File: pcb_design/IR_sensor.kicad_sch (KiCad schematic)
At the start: 32 parts, among them J6 IR_1, J7 IR_1, J8 IR_2, J9 IR_1, Q2 DMN3065LW-7, Q3 DMN3065LW-7, Q4 DMN3065LW-7, Q5 DMN3065LW-7

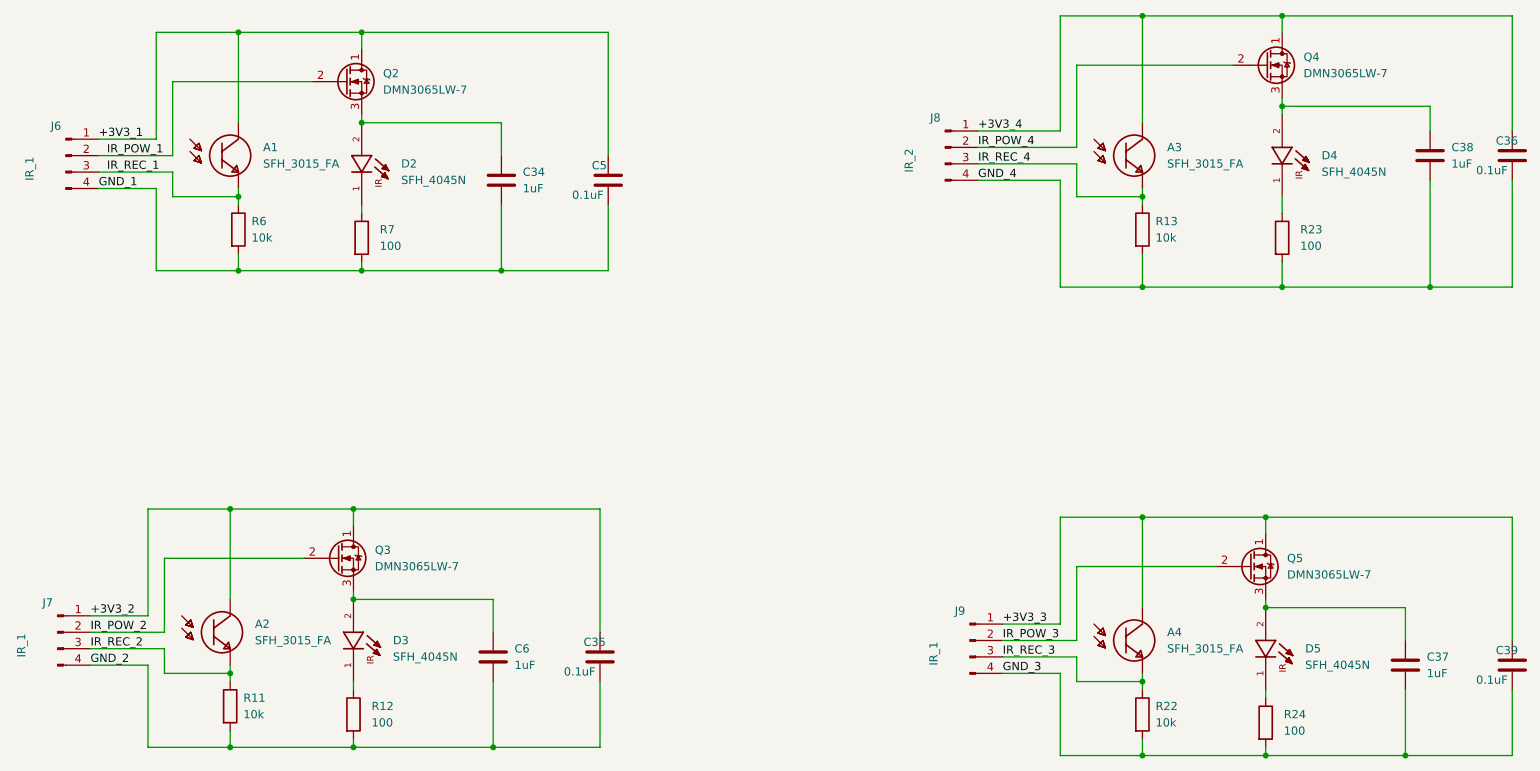
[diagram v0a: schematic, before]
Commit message: Add changes to silkscreen and filter capacitors
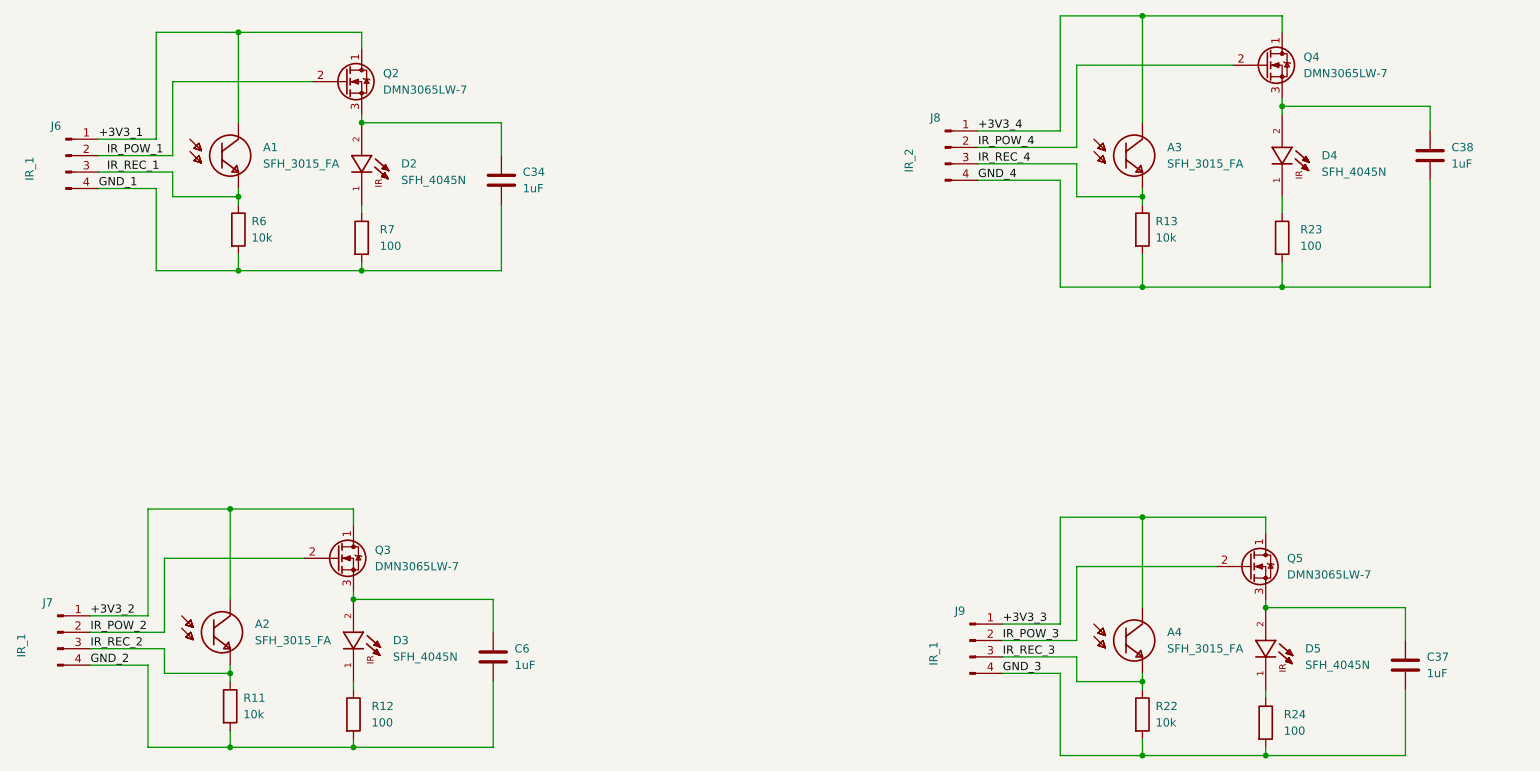
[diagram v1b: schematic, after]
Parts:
- removed C35, C36, C39, C5: 0.1uF, Capacitor_SMD:C_0402_1005Metric, symbol Device:C
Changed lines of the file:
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@@
   (junction (at 224.79 76.2) (diameter 0) (color 0 0 0 0)
   )
-  (junction (at 222.25 111.76) (diameter 0) (color 0 0 0 0)
-  )
   (junction (at 63.5 62.23) (diameter 0) (color 0 0 0 0)
   )
-  (junction (at 82.55 36.83) (diameter 0) (color 0 0 0 0)
-  )
-  (junction (at 104.14 73.66) (diameter 0) (color 0 0 0 0)
-  )
   (junction (at 62.23 135.89) (diameter 0) (color 0 0 0 0)
   )
@@
   (junction (at 63.5 36.83) (diameter 0) (color 0 0 0 0)
   )
-  (junction (at 81.28 110.49) (diameter 0) (color 0 0 0 0)
-  )
   (junction (at 203.2 148.59) (diameter 0) (color 0 0 0 0)
   )
-  (junction (at 224.79 34.29) (diameter 0) (color 0 0 0 0)
-  )
   (junction (at 203.2 34.29) (diameter 0) (color 0 0 0 0)
   )
-  (junction (at 102.87 147.32) (diameter 0) (color 0 0 0 0)
-  )
-  (junction (at 247.65 76.2) (diameter 0) (color 0 0 0 0)
-  )
   (junction (at 224.79 48.26) (diameter 0) (color 0 0 0 0)
   )
@@
   (junction (at 82.55 73.66) (diameter 0) (color 0 0 0 0)
   )
-  (junction (at 243.84 148.59) (diameter 0) (color 0 0 0 0)
-  )
   (wire (pts (xy 81.28 110.49) (xy 81.28 113.03))
     (stroke (width 0) (type default) (color 0 0 0 0))
@@
     (stroke (width 0) (type default) (color 0 0 0 0))
   )
-  (wire (pts (xy 119.38 147.32) (xy 102.87 147.32))
-    (stroke (width 0) (type default) (color 0 0 0 0))
-  )
   (wire (pts (xy 190.5 52.07) (xy 190.5 34.29))
     (stroke (width 0) (type default) (color 0 0 0 0))
@@
     (stroke (width 0) (type default) (color 0 0 0 0))
   )
-  (wire (pts (xy 260.35 138.43) (xy 260.35 148.59))
-    (stroke (width 0) (type default) (color 0 0 0 0))
-  )
   (wire (pts (xy 247.65 52.07) (xy 247.65 48.26))
     (stroke (width 0) (type default) (color 0 0 0 0))
@@
     (stroke (width 0) (type default) (color 0 0 0 0))
   )
-  (wire (pts (xy 224.79 34.29) (xy 260.35 34.29))
-    (stroke (width 0) (type default) (color 0 0 0 0))
-  )
-  (wire (pts (xy 120.65 73.66) (xy 104.14 73.66))
-    (stroke (width 0) (type default) (color 0 0 0 0))
-  )
   (wire (pts (xy 222.25 148.59) (xy 243.84 148.59))
     (stroke (width 0) (type default) (color 0 0 0 0))
   )
-  (wire (pts (xy 82.55 36.83) (xy 120.65 36.83))
-    (stroke (width 0) (type default) (color 0 0 0 0))
-  )
   (wire (pts (xy 104.14 55.88) (xy 104.14 50.8))
     (stroke (width 0) (type default) (color 0 0 0 0))
@@
     (stroke (width 0) (type default) (color 0 0 0 0))
   )
-  (wire (pts (xy 222.25 111.76) (xy 260.35 111.76))
-    (stroke (width 0) (type default) (color 0 0 0 0))
-  )
   (wire (pts (xy 203.2 111.76) (xy 222.25 111.76))
     (stroke (width 0) (type default) (color 0 0 0 0))
   )
-  (wire (pts (xy 119.38 137.16) (xy 119.38 147.32))
-    (stroke (width 0) (type default) (color 0 0 0 0))
-  )
   (wire (pts (xy 243.84 130.81) (xy 243.84 125.73))
     (stroke (width 0) (type default) (color 0 0 0 0))
@@
     (stroke (width 0) (type default) (color 0 0 0 0))
   )
-  (wire (pts (xy 260.35 59.69) (xy 260.35 76.2))
-    (stroke (width 0) (type default) (color 0 0 0 0))
-  )
   (wire (pts (xy 224.79 72.39) (xy 224.79 76.2))
     (stroke (width 0) (type default) (color 0 0 0 0))
@@
     (stroke (width 0) (type default) (color 0 0 0 0))
   )
-  (wire (pts (xy 260.35 130.81) (xy 260.35 111.76))
-    (stroke (width 0) (type default) (color 0 0 0 0))
-  )
   (wire (pts (xy 49.53 127) (xy 49.53 110.49))
     (stroke (width 0) (type default) (color 0 0 0 0))
@@
     (stroke (width 0) (type default) (color 0 0 0 0))
   )
-  (wire (pts (xy 260.35 148.59) (xy 243.84 148.59))
-    (stroke (width 0) (type default) (color 0 0 0 0))
-  )
   (wire (pts (xy 62.23 135.89) (xy 62.23 137.16))
     (stroke (width 0) (type default) (color 0 0 0 0))
@@
     (stroke (width 0) (type default) (color 0 0 0 0))
   )
-  (wire (pts (xy 120.65 63.5) (xy 120.65 73.66))
-    (stroke (width 0) (type default) (color 0 0 0 0))
-  )
   (wire (pts (xy 82.55 36.83) (xy 82.55 39.37))
     (stroke (width 0) (type default) (color 0 0 0 0))
@@
     (stroke (width 0) (type default) (color 0 0 0 0))
   )
-  (wire (pts (xy 81.28 110.49) (xy 119.38 110.49))
-    (stroke (width 0) (type default) (color 0 0 0 0))
-  )
   (wire (pts (xy 53.34 62.23) (xy 63.5 62.23))
     (stroke (width 0) (type default) (color 0 0 0 0))
@@
     (stroke (width 0) (type default) (color 0 0 0 0))
   )
-  (wire (pts (xy 260.35 76.2) (xy 247.65 76.2))
-    (stroke (width 0) (type default) (color 0 0 0 0))
-  )
   (wire (pts (xy 53.34 44.45) (xy 53.34 55.88))
     (stroke (width 0) (type default) (color 0 0 0 0))
@@
     (stroke (width 0) (type default) (color 0 0 0 0))
   )
-  (wire (pts (xy 119.38 129.54) (xy 119.38 110.49))
-    (stroke (width 0) (type default) (color 0 0 0 0))
-  )
   (wire (pts (xy 62.23 110.49) (xy 62.23 124.46))
     (stroke (width 0) (type default) (color 0 0 0 0))
@@
     (stroke (width 0) (type default) (color 0 0 0 0))
   )
-  (wire (pts (xy 260.35 52.07) (xy 260.35 34.29))
-    (stroke (width 0) (type default) (color 0 0 0 0))
-  )
   (wire (pts (xy 102.87 124.46) (xy 81.28 124.46))
     (stroke (width 0) (type default) (color 0 0 0 0))
@@
   )
   (wire (pts (xy 52.07 135.89) (xy 62.23 135.89))
-    (stroke (width 0) (type default) (color 0 0 0 0))
-  )
-  (wire (pts (xy 120.65 55.88) (xy 120.65 36.83))
     (stroke (width 0) (type default) (color 0 0 0 0))
   )
@@
     (pin "4")
   )
-  (symbol (lib_id "Device:C") (at 260.35 55.88 0) (unit 1)
-    (in_bom yes) (on_board yes)
-    (property "Reference" "C36" (id 0) (at 257.81 53.594 0)
-      (effects (font (size 1.27 1.27)) (justify left))
-    )
-    (property "Value" "0.1uF" (id 1) (at 254.762 58.166 0)
-      (effects (font (size 1.27 1.27)) (justify left))
-    )
-    (property "Footprint" "Capacitor_SMD:C_0402_1005Metric" (id 2) (at 261.3152 59.69 0)
-      (effects (font (size 1.27 1.27)) hide)
-    )
-    (property "Datasheet" "~" (id 3) (at 260.35 55.88 0)
-      (effects (font (size 1.27 1.27)) hide)
-    )
-    (pin "1")
-    (pin "2")
-  )
-  (symbol (lib_id "Device:C") (at 120.65 59.69 0) (unit 1)
-    (in_bom yes) (on_board yes)
-    (property "Reference" "C5" (id 0) (at 118.11 57.404 0)
-      (effects (font (size 1.27 1.27)) (justify left))
-    )
-    (property "Value" "0.1uF" (id 1) (at 115.062 61.976 0)
-      (effects (font (size 1.27 1.27)) (justify left))
-    )
-    (property "Footprint" "Capacitor_SMD:C_0402_1005Metric" (id 2) (at 121.6152 63.5 0)
-      (effects (font (size 1.27 1.27)) hide)
-    )
-    (property "Datasheet" "~" (id 3) (at 120.65 59.69 0)
-      (effects (font (size 1.27 1.27)) hide)
-    )
-    (pin "1")
-    (pin "2")
-  )
   (symbol (lib_id "SFH_3015_FA:SFH_3015_FA") (at 200.66 55.88 0) (unit 1)
     (in_bom yes) (on_board yes) (fields_autoplaced)
@@
     (pin "2")
   )
-  (symbol (lib_id "Device:C") (at 119.38 133.35 0) (unit 1)
-    (in_bom yes) (on_board yes)
-    (property "Reference" "C35" (id 0) (at 116.84 131.064 0)
-      (effects (font (size 1.27 1.27)) (justify left))
-    )
-    (property "Value" "0.1uF" (id 1) (at 113.792 135.636 0)
-      (effects (font (size 1.27 1.27)) (justify left))
-    )
-    (property "Footprint" "Capacitor_SMD:C_0402_1005Metric" (id 2) (at 120.3452 137.16 0)
-      (effects (font (size 1.27 1.27)) hide)
-    )
-    (property "Datasheet" "~" (id 3) (at 119.38 133.35 0)
-      (effects (font (size 1.27 1.27)) hide)
-    )
-    (pin "1")
-    (pin "2")
-  )
   (symbol (lib_id "Device:Q_NMOS_DGS") (at 219.71 119.38 0) (unit 1)
     (in_bom yes) (on_board yes) (fields_autoplaced)
@@
     (pin "3")
   )
-  (symbol (lib_id "Device:C") (at 260.35 134.62 0) (unit 1)
-    (in_bom yes) (on_board yes)
-    (property "Reference" "C39" (id 0) (at 257.81 132.334 0)
-      (effects (font (size 1.27 1.27)) (justify left))
-    )
-    (property "Value" "0.1uF" (id 1) (at 254.762 136.906 0)
-      (effects (font (size 1.27 1.27)) (justify left))
-    )
-    (property "Footprint" "Capacitor_SMD:C_0402_1005Metric" (id 2) (at 261.3152 138.43 0)
-      (effects (font (size 1.27 1.27)) hide)
-    )
-    (property "Datasheet" "~" (id 3) (at 260.35 134.62 0)
-      (effects (font (size 1.27 1.27)) hide)
-    )
-    (pin "1")
-    (pin "2")
-  )
   (symbol (lib_id "Connector:Conn_01x04_Male") (at 36.83 55.88 0) (unit 1)
